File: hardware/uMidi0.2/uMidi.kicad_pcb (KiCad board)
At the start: 2 copper layers, 66 x 40.6 mm, 49 parts, among them CON1 USB-MINI-B, IC1 6N138, IC2 ATXMEGA128A4U-M, P1 MIDI In, P2 MIDI Thru, P3 MIDI T/O, P4 MIDI Out, P5 5..12 V, P6 PDI, P7 GPIO1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

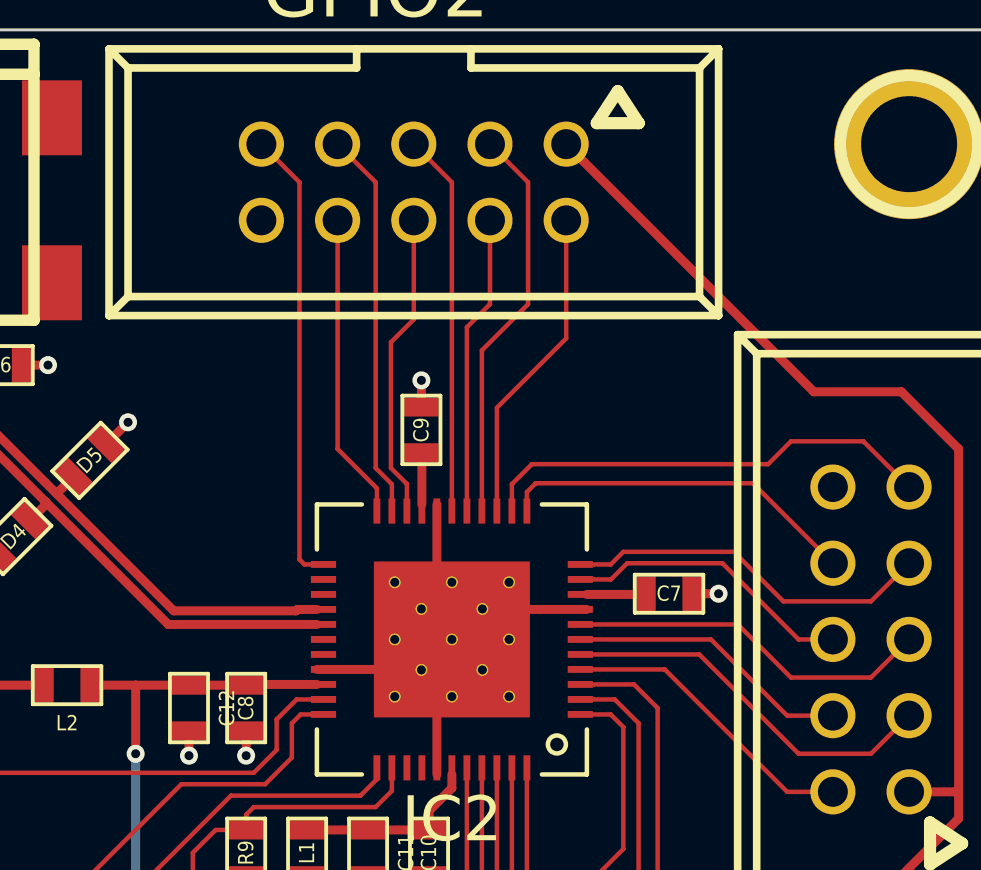
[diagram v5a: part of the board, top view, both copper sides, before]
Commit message: Route MCU power supply
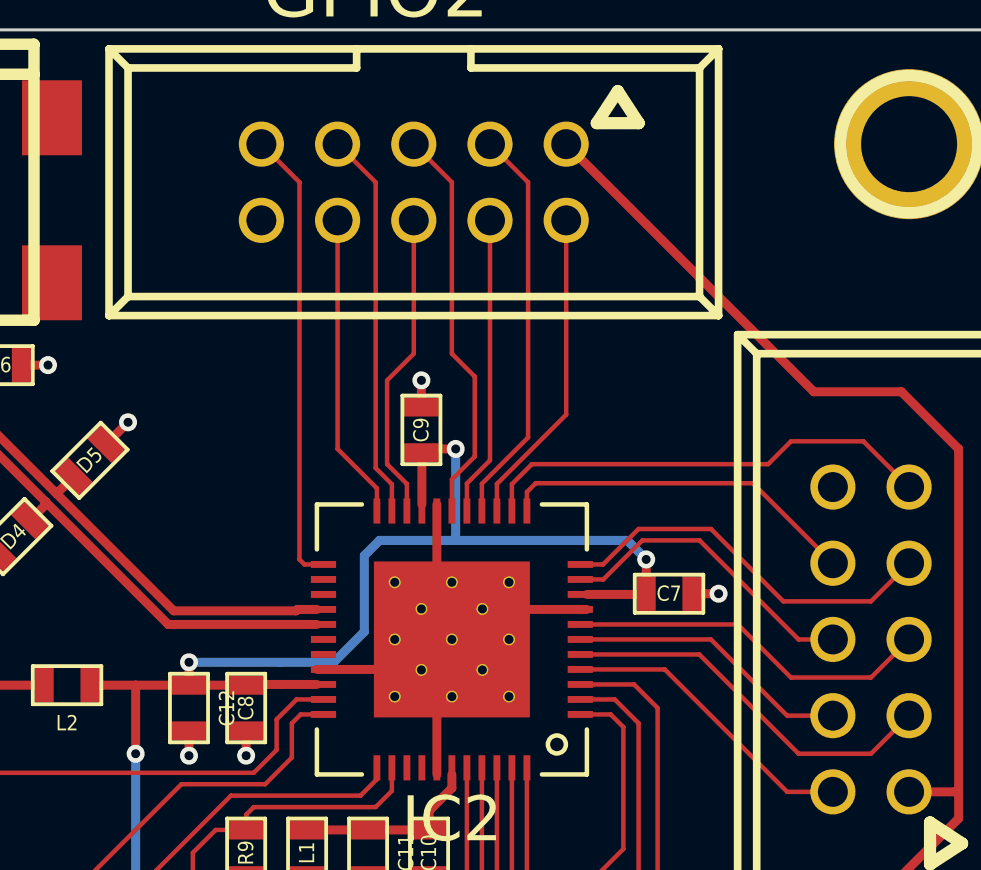
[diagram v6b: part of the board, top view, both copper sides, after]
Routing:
- net Net-(C12-Pad1): track 40.9 -> 66.0 mm, vias 2 -> 5
- net Net-(IC2-Pad11): track 12.1 -> 12.8 mm
- net Net-(IC2-Pad10): track 9.60 -> 10.2 mm
- net Net-(IC2-Pad17): track 12.5 -> 13.2 mm
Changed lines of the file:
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@@
   (general
     (links 138)
-    (no_connects 3)
+    (no_connects 1)
     (area 67.259999 123.139999 133.400001 163.880001)
     (thickness 1.6)
     (drawings 4)
-    (tracks 408)
+    (tracks 432)
     (zones 0)
     (modules 49)
@@
   (segment (start 111.506 149.86) (end 113.538 149.86) (width 0.3) (layer F.Cu) (net 4))
   (segment (start 109.474 149.86) (end 111.506 149.86) (width 0.3) (layer F.Cu) (net 4))
+  (segment (start 108.585 144.272) (end 105.537 144.272) (width 0.3) (layer B.Cu) (net 5))
+  (segment (start 108.585 144.272) (end 110.363 144.272) (width 0.3) (layer B.Cu) (net 5))
+  (segment (start 110.363 144.272) (end 111.379 143.256) (width 0.3) (layer B.Cu) (net 5))
+  (segment (start 111.379 143.256) (end 111.379 140.716) (width 0.3) (layer B.Cu) (net 5))
+  (segment (start 111.379 140.716) (end 111.887 140.208) (width 0.3) (layer B.Cu) (net 5))
+  (segment (start 114.427 140.208) (end 111.887 140.208) (width 0.3) (layer B.Cu) (net 5))
+  (segment (start 105.537 144.272) (end 105.537 145.034) (width 0.3) (layer F.Cu) (net 5) (status 800000))
+  (via (at 105.537 144.272) (size 0.6) (layers F.Cu B.Cu) (net 5))
+  (segment (start 113.284 137.287) (end 113.411 137.16) (width 0.3) (layer F.Cu) (net 5))
+  (segment (start 113.411 137.16) (end 114.427 137.16) (width 0.3) (layer F.Cu) (net 5))
+  (segment (start 114.427 137.16) (end 114.427 140.208) (width 0.3) (layer B.Cu) (net 5))
+  (via (at 114.427 137.16) (size 0.6) (layers F.Cu B.Cu) (net 5))
+  (segment (start 114.427 140.208) (end 114.427 140.081) (width 0.3) (layer B.Cu) (net 5))
+  (segment (start 114.427 140.081) (end 114.427 140.208) (width 0.3) (layer B.Cu) (net 5))
+  (segment (start 119.634 140.208) (end 120.142 140.208) (width 0.3) (layer B.Cu) (net 5))
+  (segment (start 114.427 140.208) (end 119.634 140.208) (width 0.3) (layer B.Cu) (net 5))
+  (segment (start 120.777 140.843) (end 120.777 141.986) (width 0.3) (layer F.Cu) (net 5))
+  (via (at 120.777 140.843) (size 0.6) (layers F.Cu B.Cu) (net 5))
+  (segment (start 120.142 140.208) (end 120.777 140.843) (width 0.3) (layer B.Cu) (net 5))
   (segment (start 103.759 145.034) (end 103.759 147.32) (width 0.3) (layer F.Cu) (net 5))
   (segment (start 103.759 147.32) (end 103.759 153.289) (width 0.3) (layer B.Cu) (net 5))
@@
   (segment (start 105.537 145.034) (end 103.759 145.034) (width 0.3) (layer F.Cu) (net 5))
   (segment (start 103.759 145.034) (end 102.235 145.034) (width 0.3) (layer F.Cu) (net 5))
-  (segment (start 109.8 145.01) (end 107.466 145.01) (width 0.3) (layer F.Cu) (net 5))
+  (segment (start 109.8 145.01) (end 108.585 145.01) (width 0.3) (layer F.Cu) (net 5))
+  (segment (start 108.585 145.01) (end 107.466 145.01) (width 0.3) (layer F.Cu) (net 5))
   (segment (start 107.466 145.01) (end 107.442 145.034) (width 0.3) (layer F.Cu) (net 5))
   (segment (start 107.442 145.034) (end 105.537 145.034) (width 0.3) (layer F.Cu) (net 5))
@@
   (segment (start 128.27 144.78) (end 129.54 143.51) (width 0.15) (layer F.Cu) (net 20))
   (segment (start 125.603 144.78) (end 128.27 144.78) (width 0.15) (layer F.Cu) (net 20))
-  (segment (start 118.8 141.51) (end 119.602 141.51) (width 0.15) (layer F.Cu) (net 21))
+  (segment (start 118.8 141.51) (end 119.348 141.51) (width 0.15) (layer F.Cu) (net 21))
+  (segment (start 119.348 141.51) (end 120.65 140.208) (width 0.15) (layer F.Cu) (net 21))
   (segment (start 125.857 143.51) (end 127 143.51) (width 0.15) (layer F.Cu) (net 21))
-  (segment (start 123.317 140.97) (end 125.857 143.51) (width 0.15) (layer F.Cu) (net 21))
-  (segment (start 120.142 140.97) (end 123.317 140.97) (width 0.15) (layer F.Cu) (net 21))
-  (segment (start 119.602 141.51) (end 120.142 140.97) (width 0.15) (layer F.Cu) (net 21))
+  (segment (start 122.555 140.208) (end 125.857 143.51) (width 0.15) (layer F.Cu) (net 21))
+  (segment (start 120.65 140.208) (end 122.555 140.208) (width 0.15) (layer F.Cu) (net 21))
   (segment (start 126.873 143.51) (end 127 143.51) (width 0.15) (layer F.Cu) (net 21) (status 20))
-  (segment (start 118.8 141.01) (end 119.594 141.01) (width 0.15) (layer F.Cu) (net 22))
-  (segment (start 119.594 141.01) (end 120.015 140.589) (width 0.15) (layer F.Cu) (net 22))
+  (segment (start 118.8 141.01) (end 119.34 141.01) (width 0.15) (layer F.Cu) (net 22))
+  (segment (start 119.34 141.01) (end 120.523 139.827) (width 0.15) (layer F.Cu) (net 22))
+  (segment (start 120.523 139.827) (end 122.936 139.827) (width 0.15) (layer F.Cu) (net 22))
   (segment (start 128.27 142.24) (end 129.54 140.97) (width 0.15) (layer F.Cu) (net 22))
   (segment (start 125.349 142.24) (end 128.27 142.24) (width 0.15) (layer F.Cu) (net 22))
-  (segment (start 123.698 140.589) (end 125.349 142.24) (width 0.15) (layer F.Cu) (net 22))
-  (segment (start 120.015 140.589) (end 123.698 140.589) (width 0.15) (layer F.Cu) (net 22))
+  (segment (start 122.936 139.827) (end 125.349 142.24) (width 0.15) (layer F.Cu) (net 22))
   (segment (start 116.8 139.01) (end 116.8 138.597) (width 0.15) (layer F.Cu) (net 23))
   (segment (start 124.333 138.303) (end 127 140.97) (width 0.15) (layer F.Cu) (net 23))
@@
   (segment (start 116.967 137.668) (end 124.841 137.668) (width 0.15) (layer F.Cu) (net 24))
   (segment (start 116.3 138.335) (end 116.967 137.668) (width 0.15) (layer F.Cu) (net 24))
-  (segment (start 115.8 139.01) (end 115.8 135.787) (width 0.15) (layer F.Cu) (net 25))
-  (segment (start 118.11 133.477) (end 118.11 129.54) (width 0.15) (layer F.Cu) (net 25))
-  (segment (start 115.8 135.787) (end 118.11 133.477) (width 0.15) (layer F.Cu) (net 25))
-  (segment (start 115.3 139.01) (end 115.3 133.874) (width 0.15) (layer F.Cu) (net 26))
+  (segment (start 115.8 139.01) (end 115.8 138.327) (width 0.15) (layer F.Cu) (net 25))
+  (segment (start 118.11 136.017) (end 118.11 129.54) (width 0.15) (layer F.Cu) (net 25))
+  (segment (start 115.8 138.327) (end 118.11 136.017) (width 0.15) (layer F.Cu) (net 25))
+  (segment (start 115.3 139.01) (end 115.3 138.319) (width 0.15) (layer F.Cu) (net 26))
   (segment (start 116.84 128.27) (end 115.57 127) (width 0.15) (layer F.Cu) (net 26))
-  (segment (start 116.84 132.334) (end 116.84 128.27) (width 0.15) (layer F.Cu) (net 26))
-  (segment (start 115.3 133.874) (end 116.84 132.334) (width 0.15) (layer F.Cu) (net 26))
-  (segment (start 114.8 139.01) (end 114.8 133.104) (width 0.15) (layer F.Cu) (net 27))
-  (segment (start 115.57 132.334) (end 115.57 129.54) (width 0.15) (layer F.Cu) (net 27))
-  (segment (start 114.8 133.104) (end 115.57 132.334) (width 0.15) (layer F.Cu) (net 27))
-  (segment (start 114.3 139.01) (end 114.3 128.27) (width 0.15) (layer F.Cu) (net 28))
+  (segment (start 116.84 136.779) (end 116.84 128.27) (width 0.15) (layer F.Cu) (net 26))
+  (segment (start 115.3 138.319) (end 116.84 136.779) (width 0.15) (layer F.Cu) (net 26))
+  (segment (start 114.8 139.01) (end 114.8 138.311) (width 0.15) (layer F.Cu) (net 27))
+  (segment (start 115.57 137.541) (end 115.57 129.54) (width 0.15) (layer F.Cu) (net 27))
+  (segment (start 114.8 138.311) (end 115.57 137.541) (width 0.15) (layer F.Cu) (net 27))
+  (segment (start 114.3 139.01) (end 114.3 138.176) (width 0.15) (layer F.Cu) (net 28))
   (segment (start 114.3 128.27) (end 113.03 127) (width 0.15) (layer F.Cu) (net 28))
+  (segment (start 114.3 133.985) (end 114.3 128.27) (width 0.15) (layer F.Cu) (net 28))
+  (segment (start 115.062 134.747) (end 114.3 133.985) (width 0.15) (layer F.Cu) (net 28))
+  (segment (start 115.062 137.414) (end 115.062 134.747) (width 0.15) (layer F.Cu) (net 28))
+  (segment (start 114.3 138.176) (end 115.062 137.414) (width 0.15) (layer F.Cu) (net 28))
   (segment (start 112.8 139.01) (end 112.8 138.327) (width 0.15) (layer F.Cu) (net 29))
-  (segment (start 113.03 132.842) (end 113.03 129.54) (width 0.15) (layer F.Cu) (net 29))
-  (segment (start 112.268 133.604) (end 113.03 132.842) (width 0.15) (layer F.Cu) (net 29))
-  (segment (start 112.268 137.795) (end 112.268 133.604) (width 0.15) (layer F.Cu) (net 29))
-  (segment (start 112.8 138.327) (end 112.268 137.795) (width 0.15) (layer F.Cu) (net 29))
+  (segment (start 113.03 133.985) (end 113.03 129.54) (width 0.15) (layer F.Cu) (net 29))
+  (segment (start 112.141 134.874) (end 113.03 133.985) (width 0.15) (layer F.Cu) (net 29))
+  (segment (start 112.141 137.668) (end 112.141 134.874) (width 0.15) (layer F.Cu) (net 29))
+  (segment (start 112.8 138.327) (end 112.141 137.668) (width 0.15) (layer F.Cu) (net 29))
   (segment (start 112.3 139.01) (end 112.3 138.335) (width 0.15) (layer F.Cu) (net 30))
   (segment (start 111.76 128.27) (end 110.49 127) (width 0.15) (layer F.Cu) (net 30))

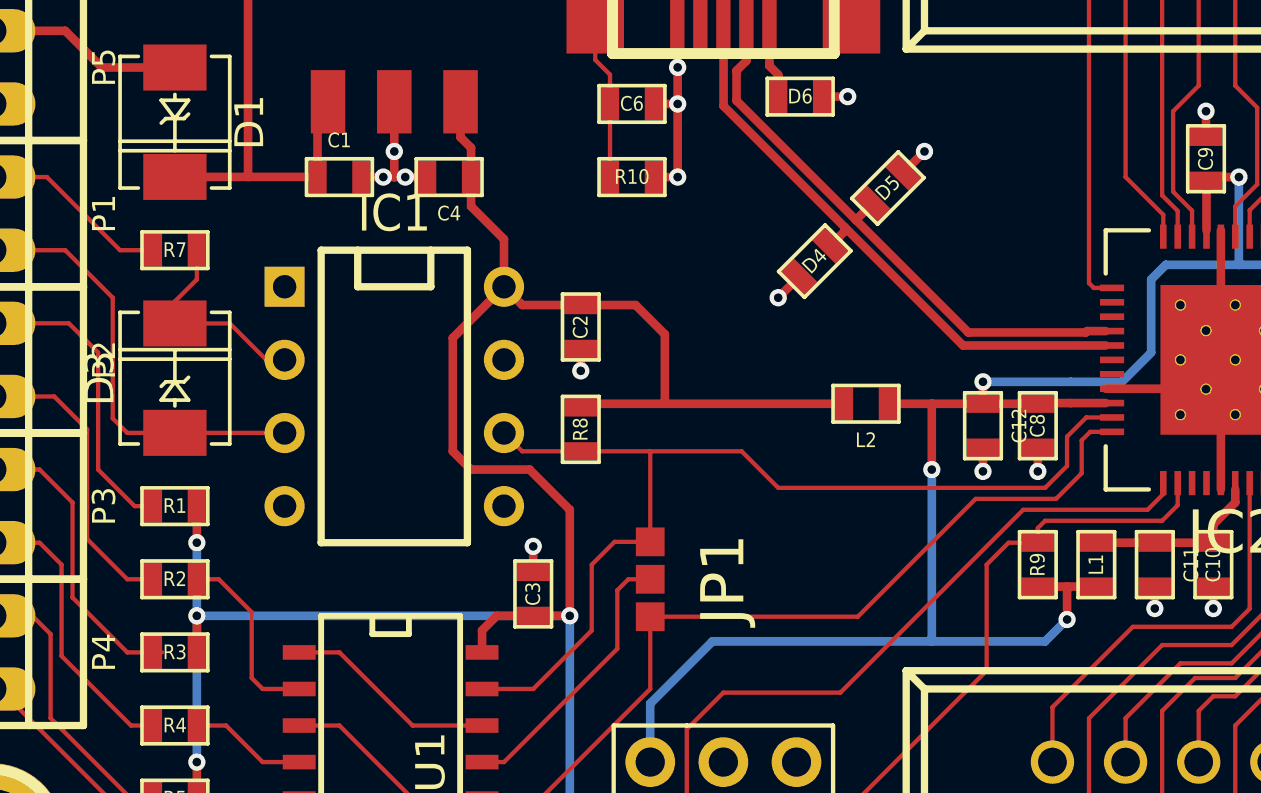
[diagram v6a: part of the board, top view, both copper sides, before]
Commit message: Use SMD package for optocoupler
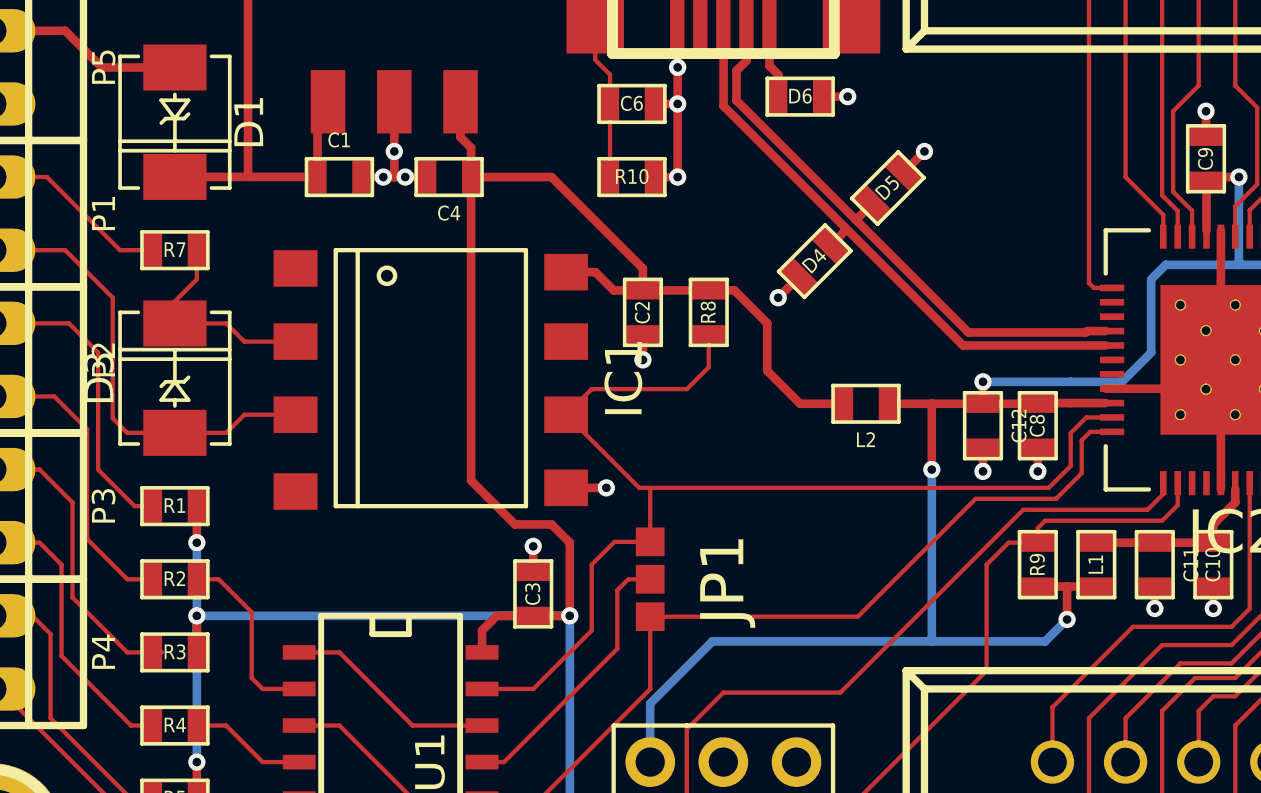
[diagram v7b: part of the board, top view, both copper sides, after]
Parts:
- IC1: footprint Sockets_DIP:DIP-8__300 -> Opto:Optocoupler_DIP8_SMD
- moved R8 6.02 mm to (96.0, 141.9)
- moved C2 2.22 mm to (93.7, 141.9)
- moved IC1 1.42 mm to (86.4, 144.1)
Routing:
- net RXD: track 35.7 -> 39.4 mm
- net GND: track 44.8 -> 46.3 mm, vias 20 -> 21
- net +3.3V: track 155.3 -> 156.1 mm
- net Net-(D3-Pad1): track 15.2 -> 15.9 mm

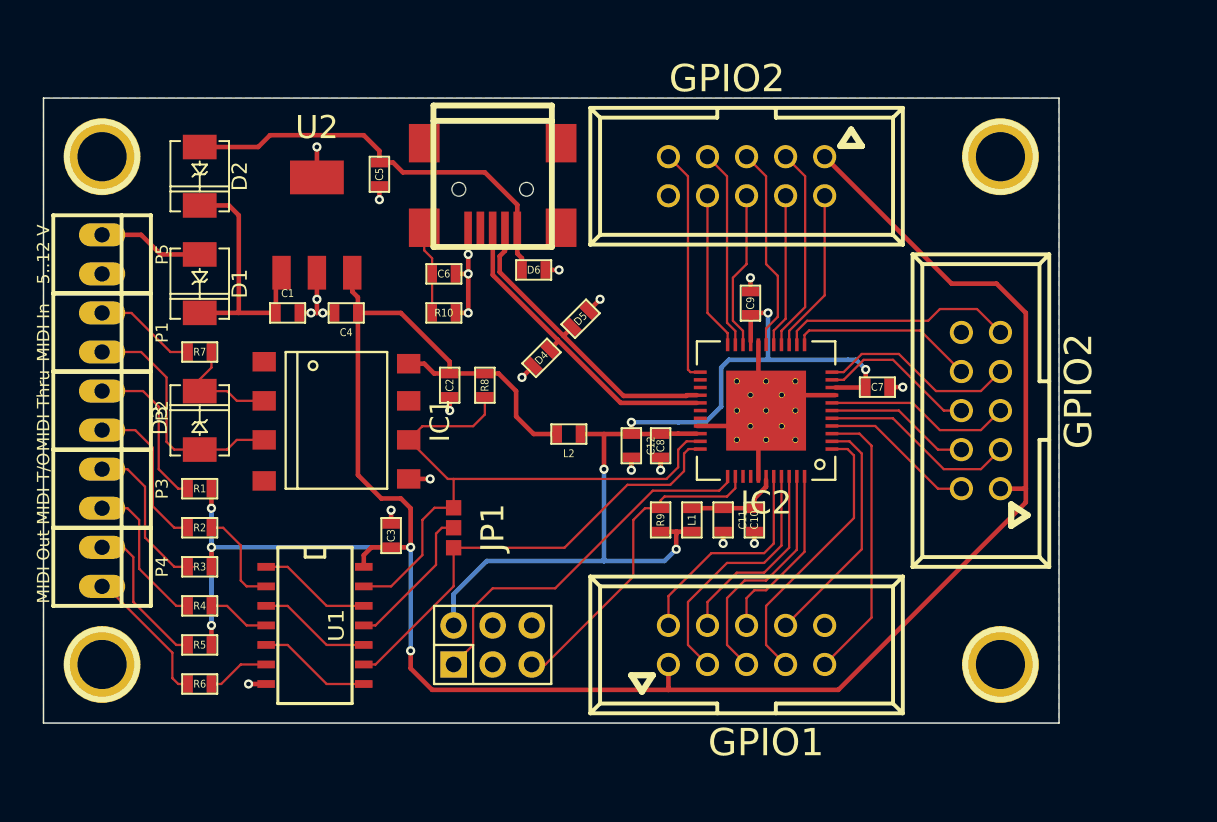
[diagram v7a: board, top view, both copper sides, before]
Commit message: Add filters to GPIO pwr supply
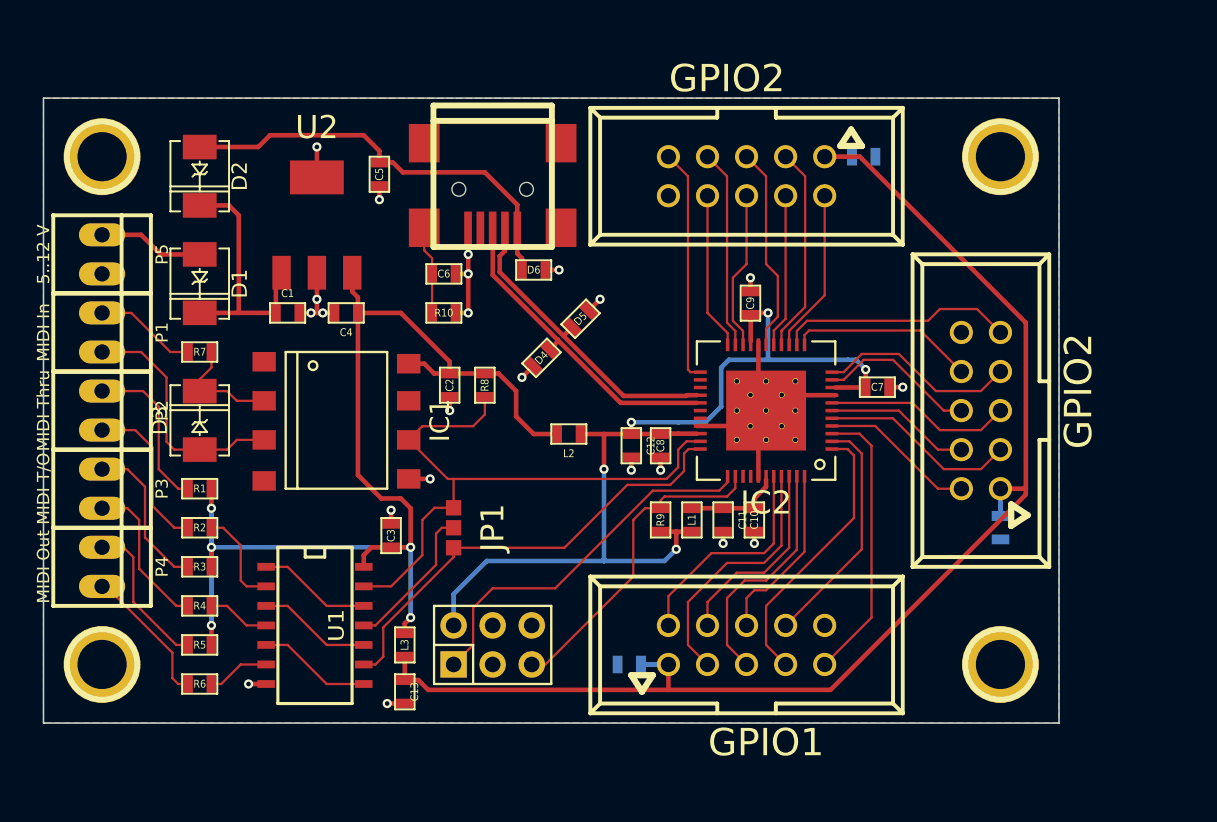
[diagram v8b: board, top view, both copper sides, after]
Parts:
- added C13: 10u, SMD_Packages:SMD-0603, F.Cu at (90.8, 161.8)
- added C14: 100n, SMD_Packages:SMD-0603, B.Cu at (105.4, 160.0)
- added C15: 100n, SMD_Packages:SMD-0603, B.Cu at (129.5, 151.1)
- added C16: 100n, SMD_Packages:SMD-0603, B.Cu at (120.7, 127.0)
- added L3: 10u, SMD_Packages:SMD-0603, F.Cu at (90.8, 158.8)
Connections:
- P7 pad 1: +3.3V -> VGPIO
- P8 pad 1: +3.3V -> VGPIO
- P9 pad 1: +3.3V -> VGPIO
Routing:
- net VGPIO: track 0.00 -> 85.1 mm
- net +3.3V: track 156.1 -> 74.9 mm
- net GND: track 46.3 -> 47.5 mm, vias 21 -> 22
